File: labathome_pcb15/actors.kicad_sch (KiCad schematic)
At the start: 39 parts, among them J18 K1, J24 K1, J7 FAN5V, J8 3V GN RGB 5V, K1 G6K-2, Q1 BC817, Q2 IRLML6344, Q3 TIP41, Q4 BC817, Q5 IRLML6344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

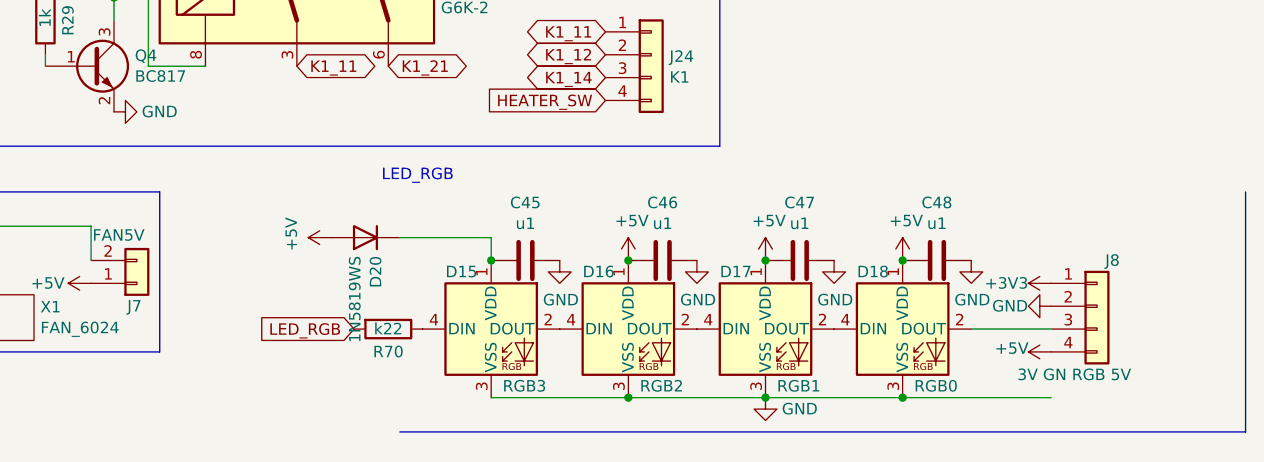
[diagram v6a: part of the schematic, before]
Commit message: Updates in PCB, arduino test firmware
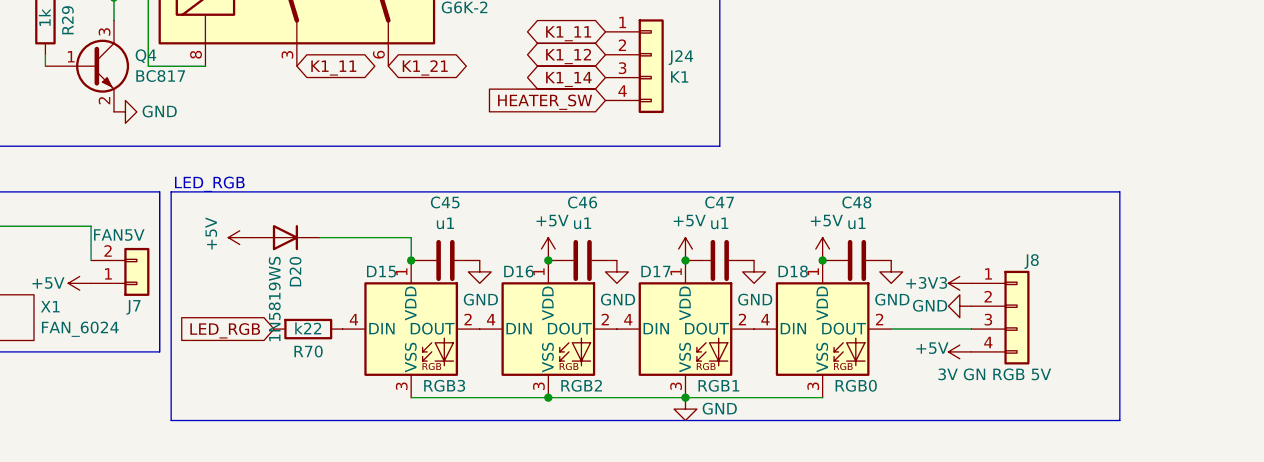
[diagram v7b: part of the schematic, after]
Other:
- company: (none) -> Klaus Liebler
- title: (none) -> lab@home
- moved on the sheet: C45, C46, C47, C48, D15, D16, D17, D18, D20, J8, R70

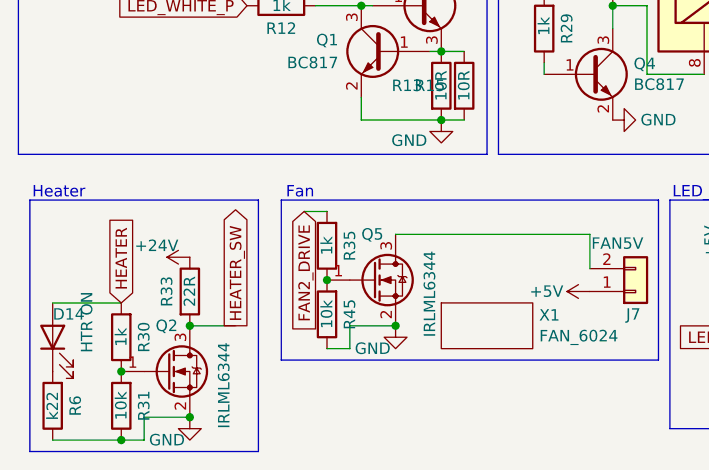
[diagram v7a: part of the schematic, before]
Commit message: Re-enumerate Servos and Fans
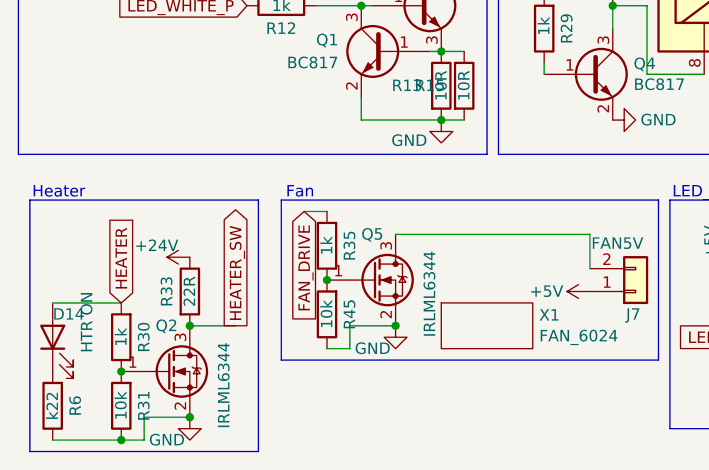
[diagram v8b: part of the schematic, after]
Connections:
- net FAN2_DRIVE renamed FAN_DRIVE
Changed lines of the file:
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@@
 		)
 	)
-	(global_label "FAN2_DRIVE"
+	(global_label "FAN_DRIVE"
 		(shape input)
 		(at 45.72 55.88 270)
@@
 		)
 		(property "Intersheetrefs" "${INTERSHEET_REFS}"
-			(at 45.72 69.1988 90)
+			(at 45.72 68.7229 90)
 			(effects
 				(font
